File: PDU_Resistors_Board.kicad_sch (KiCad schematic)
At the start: 35 parts, among them J1 To_Control_Board

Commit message: VER1.0: отправил в резонит на проверку
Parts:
- removed J1: To_Control_Board, Connector_Molex:Molex_Mini-Fit_Jr_5566-06A_2x03_P4.20mm_Vertical, symbol Connector_Generic:Conn_02x03_Top_Bottom
- removed R10, R11, R12, R13, R14, R15, R24, R25, R26, R27, R28, R29, R30, R9: 20k, Resistor_THT:R_Axial_Power_L60.0mm_W14.0mm_P66.04mm, symbol Device:R
- added J1: VDC_IN, Connector_Molex:Molex_Mini-Fit_Jr_5566-02A_2x01_P4.20mm_Vertical, symbol Connector_Generic:Conn_01x02
- added J2: VDC_OUT1, Connector_Molex:Molex_Mini-Fit_Jr_5566-02A_2x01_P4.20mm_Vertical, symbol Connector_Generic:Conn_01x02
- added J3: VDC_OUT2, Connector_Molex:Molex_Mini-Fit_Jr_5566-02A_2x01_P4.20mm_Vertical, symbol Connector_Generic:Conn_01x02
- R1, R2, R3, R4, R5, R6, R7, R8: value 20k -> 10k
- R10: renamed from R17; value 20k -> 10k
- R11: renamed from R18; value 20k -> 10k
- R12: renamed from R19; value 20k -> 10k
- R13: renamed from R20; value 20k -> 10k
- R14: renamed from R21; value 20k -> 10k
- R15: renamed from R22; value 20k -> 10k
- R16: renamed from R23; value 20k -> 10k
- R9: renamed from R16; value 20k -> 10k
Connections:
- net VDC_IN: now also J1.1 (Pin_1), J1.2 (Pin_2)
- net VDC_OUT1_Relay: now also J3.1 (Pin_1), J3.2 (Pin_2)
- net VDC_OUT2_Relay: now also J2.1 (Pin_1), J2.2 (Pin_2)

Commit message: VER1.0: длбавил схему в доки
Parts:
- J1: value VDC_IN -> ~; Product Name (none) -> DS1073-01-2x1-MVT6; Purpose (none) -> VDC_IN
- J2: value VDC_OUT1 -> ~; Product Name (none) -> DS1073-01-2x1-MVT6; Purpose (none) -> VDC_OUT1
- J3: value VDC_OUT2 -> ~; Product Name (none) -> DS1073-01-2x1-MVT6; Purpose (none) -> VDC_OUT2
- R1, R10, R11, R12, R13, R14, R15, R16, R2, R3, R4, R5, R6, R7, R8, R9: Product Name (none) -> SQP 20 Вт

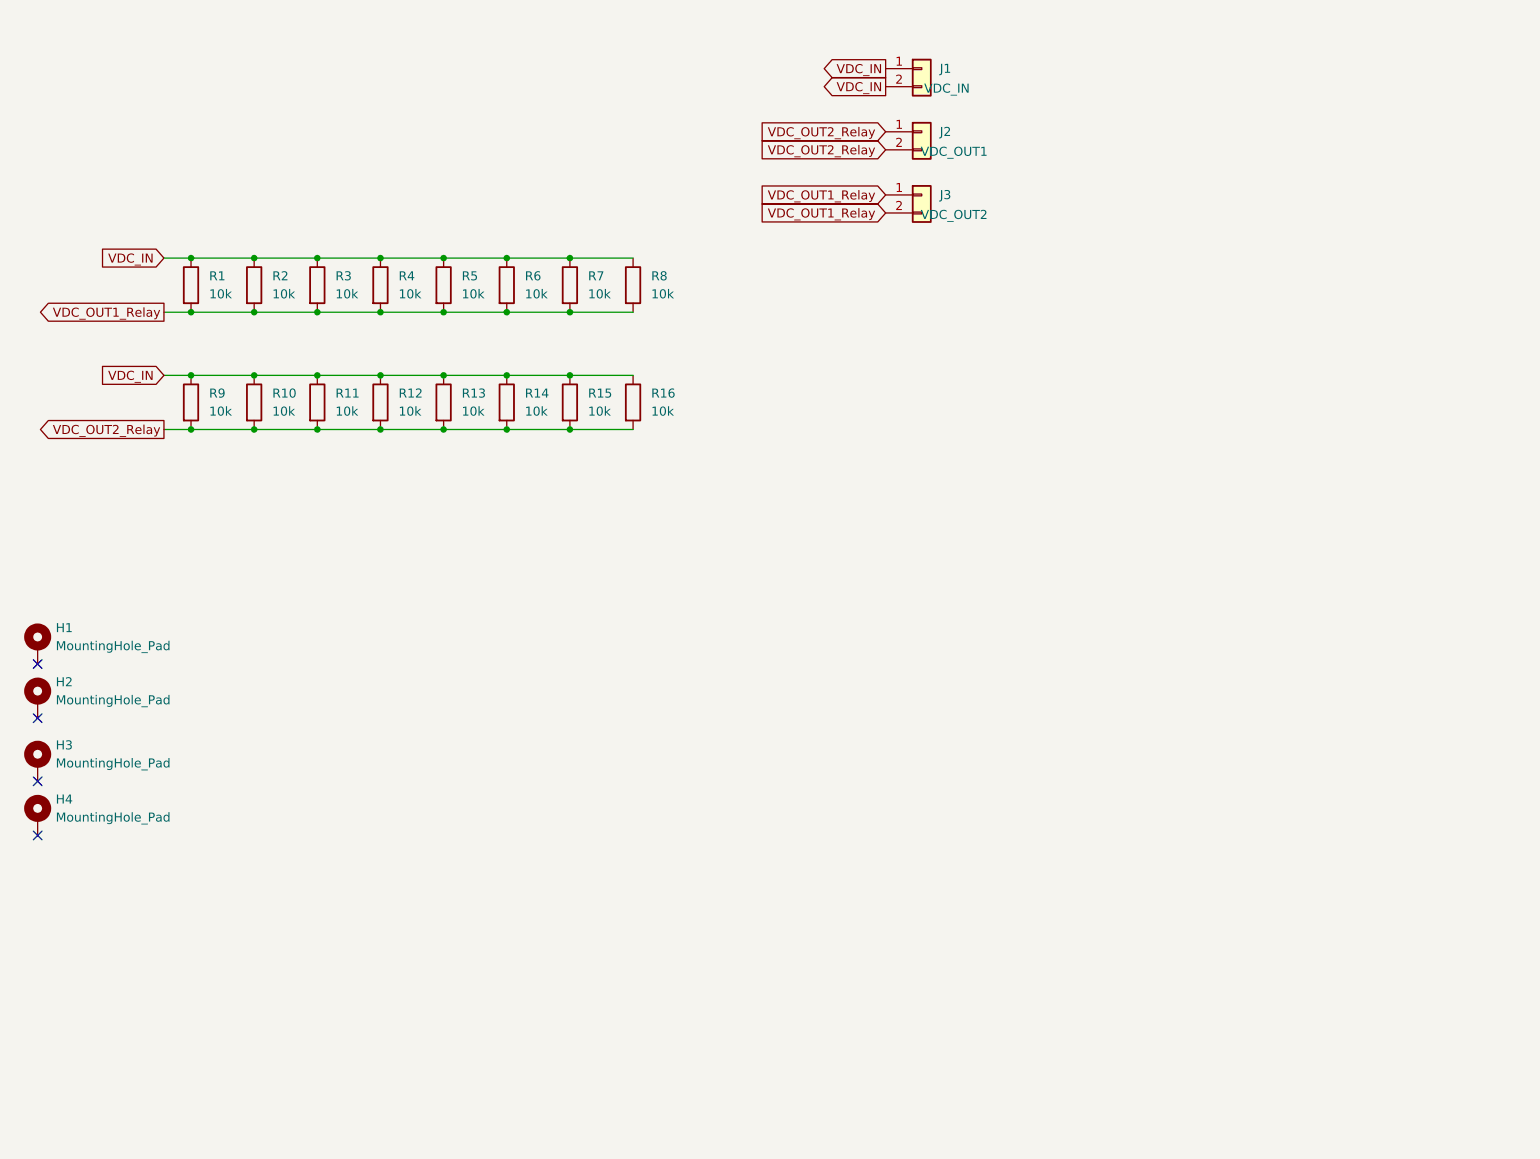
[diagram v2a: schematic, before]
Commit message: VER1.0: добавил схему по госту в доки
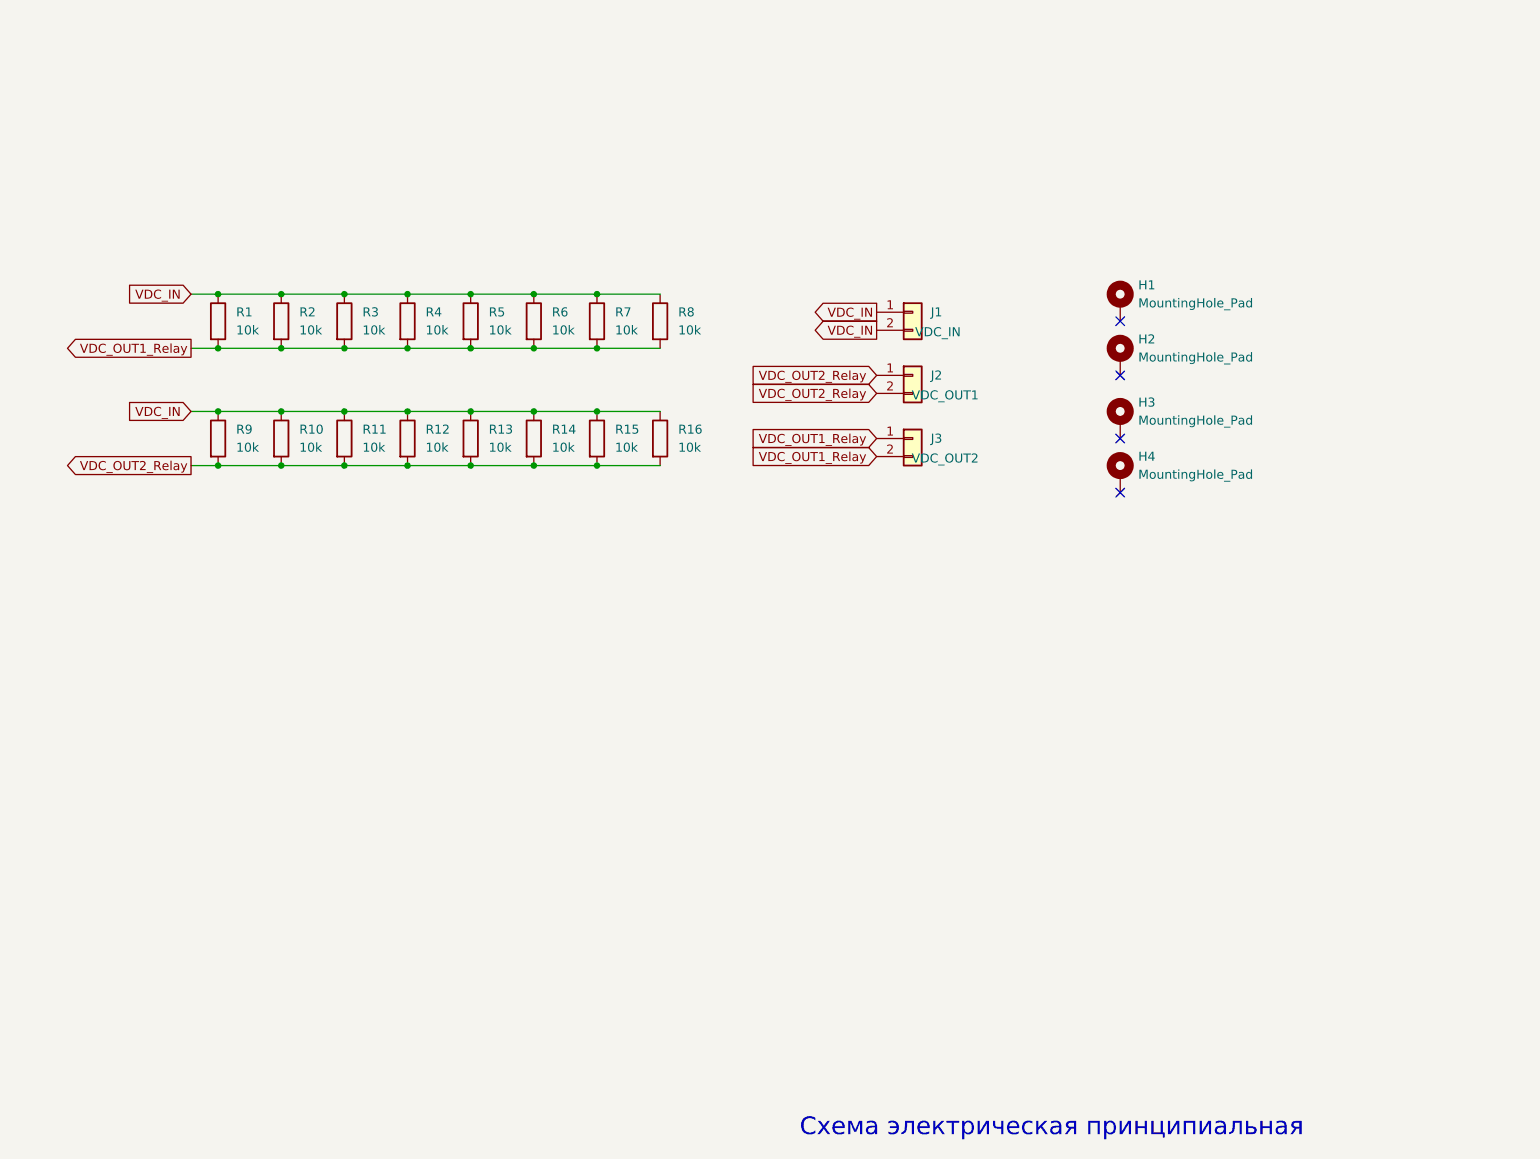
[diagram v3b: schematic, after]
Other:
- note added: "Схема электрическая принципиальная"
- company: (none) -> ООО "Электротранспортные технологии"
- title: (none) -> Плата предзаряда резисторов
- moved on the sheet: H1, H2, H3, H4, J1, J2, J3, R1, R10, R11, R12, R13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
